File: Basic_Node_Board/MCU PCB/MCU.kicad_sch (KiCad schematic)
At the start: 34 parts, among them J1 Conn_01x02, J2 Conn_01x06_Socket, J3 Conn_01x19_Socket, J4 Conn_01x02_Pin, J5 Conn_01x03_Socket, U2 ESP32-DEVKIT-C, U3 TPS54560BQDDARQ1, U4 AP64060WU-7, U5 AP64060WU-7, U6 TJA1050T/CM,118

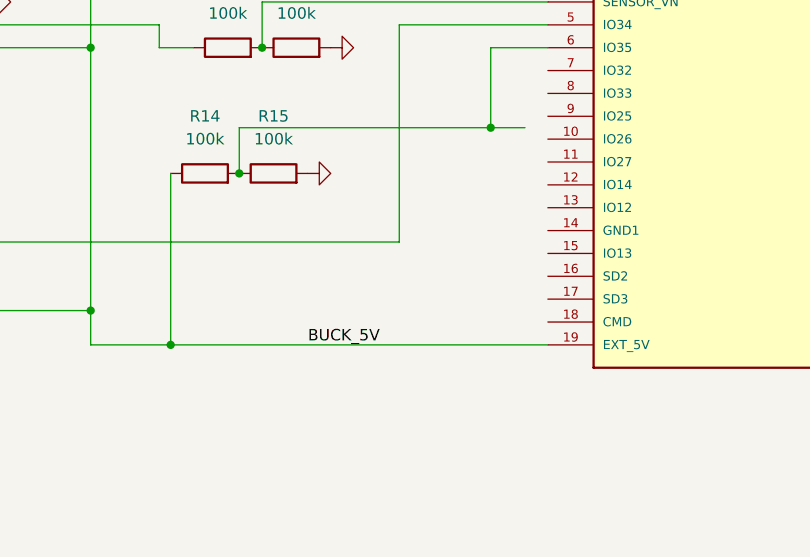
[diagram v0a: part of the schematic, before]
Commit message: made changes to some footprints and overall layout of the board (in line with TI buck recomendations)
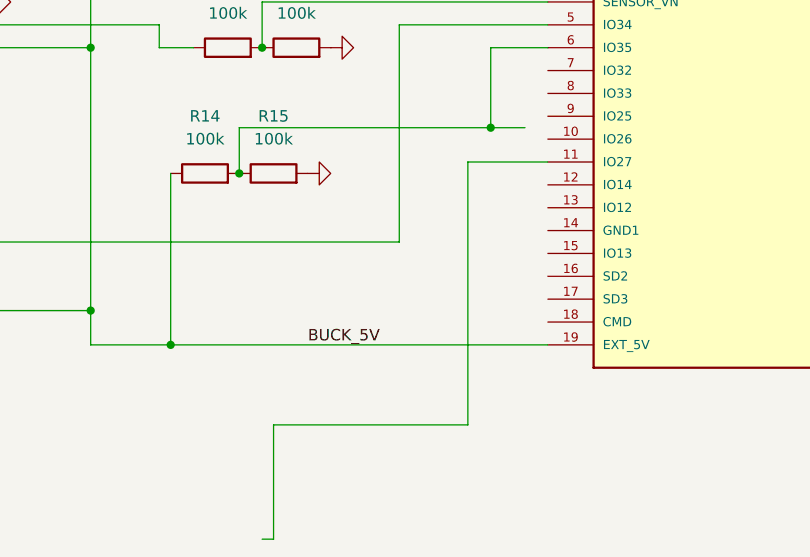
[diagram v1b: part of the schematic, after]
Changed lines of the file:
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@@
+	(wire
+		(pts
+			(xy 100.33 134.62) (xy 91.44 134.62)
+		)
+		(stroke
+			(width 0)
+			(type default)
+		)
+	)
 	(wire
 		(pts
@@
 	(wire
 		(pts
+			(xy 69.85 163.83) (xy 91.44 163.83)
+		)
+		(stroke
+			(width 0)
+			(type default)
+		)
+	)
+	(wire
+		(pts
 			(xy 246.38 46.99) (xy 255.27 46.99)
 		)
@@
 	(wire
 		(pts
+			(xy 91.44 134.62) (xy 91.44 163.83)
+		)
+		(stroke
+			(width 0)
+			(type default)
+		)
+	)
+	(wire
+		(pts
 			(xy 261.62 139.7) (xy 262.89 139.7)
 		)
@@
 	(wire
 		(pts
+			(xy 68.58 176.53) (xy 69.85 176.53)
+		)
+		(stroke
+			(width 0)
+			(type default)
+		)
+	)
+	(wire
+		(pts
 			(xy 57.15 121.92) (xy 57.15 119.38)
 		)
@@
 		)
 		(stroke
+			(width 0)
+			(type default)
+		)
+	)
+	(wire
+		(pts
+			(xy 69.85 163.83) (xy 69.85 176.53)
+		)
+		(stroke

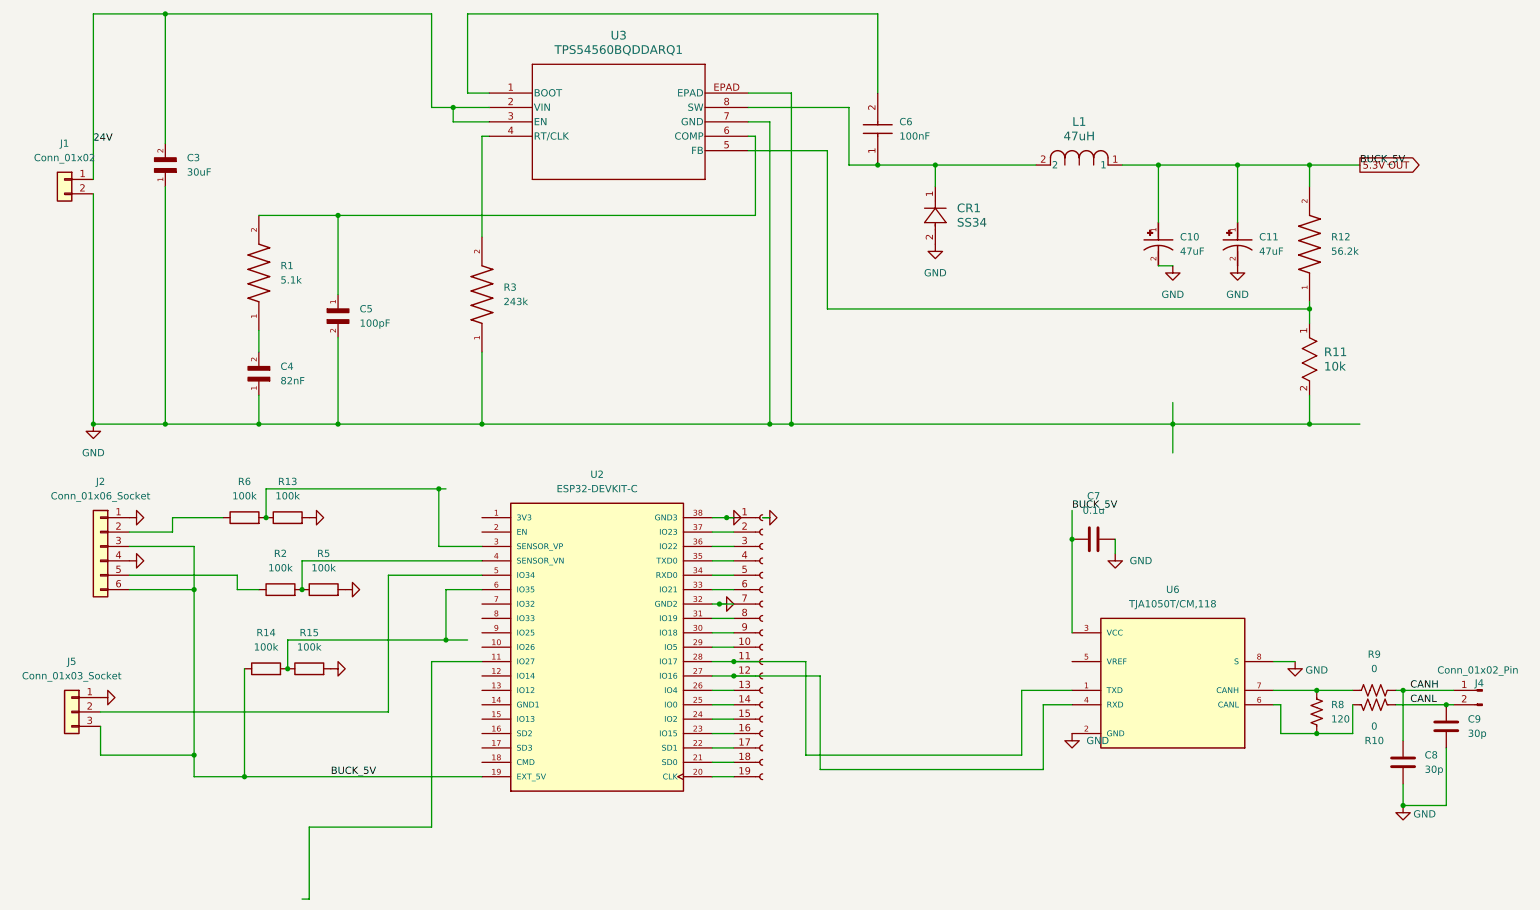
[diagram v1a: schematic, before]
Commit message: fixed the buck converter
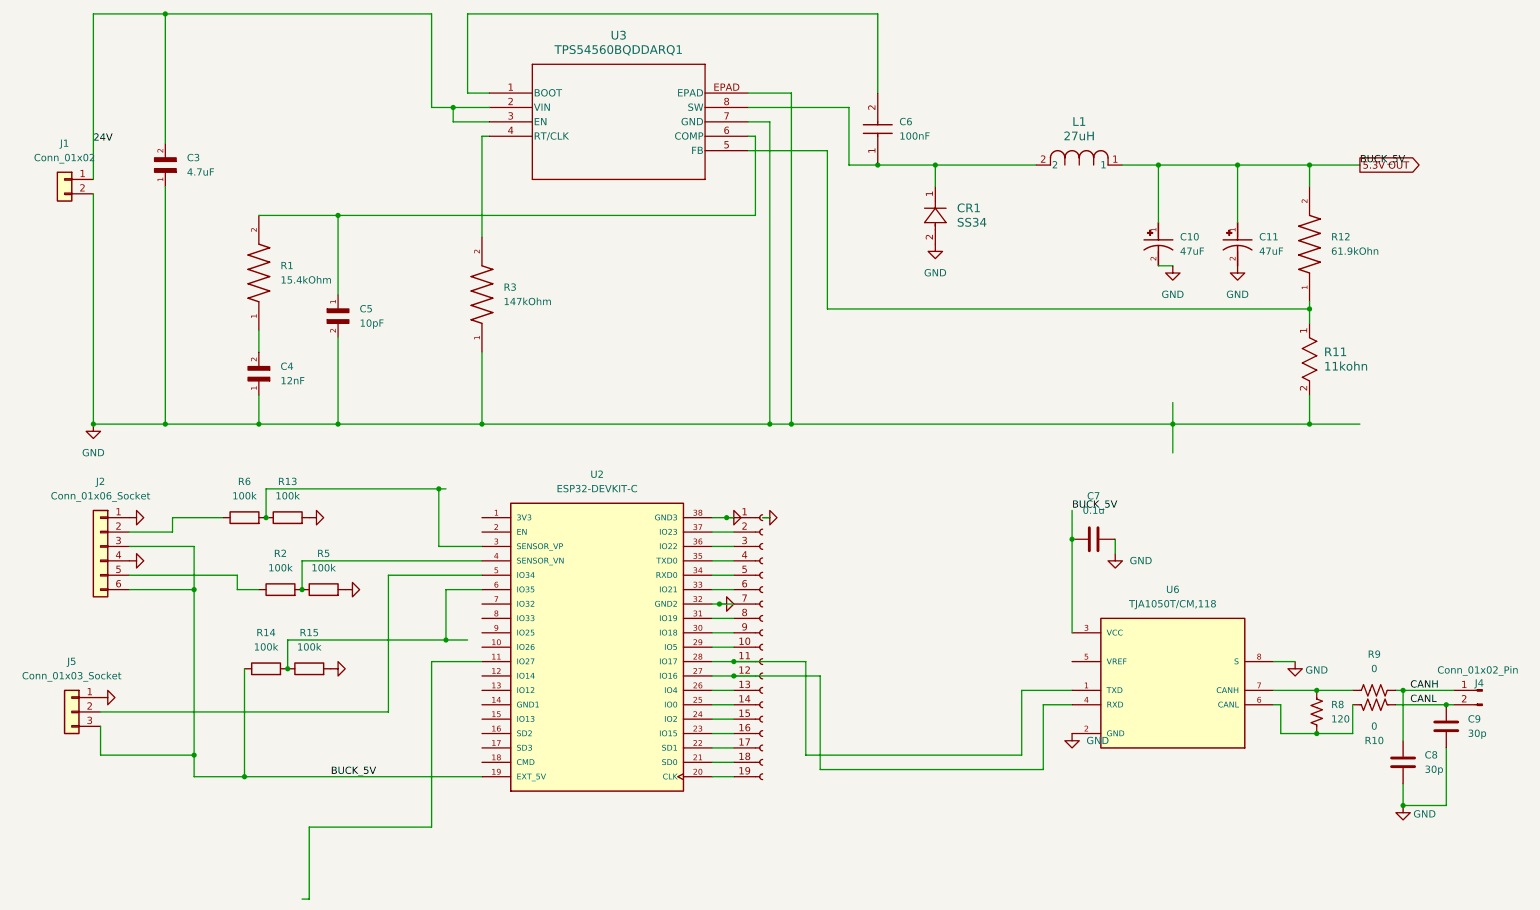
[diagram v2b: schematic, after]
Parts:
- C3: value 30uF -> 4.7uF
- C4: value 82nF -> 12nF
- C5: value 100pF -> 10pF
- L1: value 47uH -> 27uH
- R1: value 5.1k -> 15.4kOhm
- R11: value 10k -> 11kohn
- R12: value 56.2k -> 61.9kOhn
- R3: value 243k -> 147kOhm
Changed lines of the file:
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@@
 			)
 		)
-		(property "Value" "243k"
+		(property "Value" "147kOhm"
 			(at 104.14 71.1199 90)
 			(effects
@@
 			)
 		)
-		(property "Value" "82nF"
+		(property "Value" "12nF"
 			(at 64.77 85.0899 90)
 			(effects
@@
 			)
 		)
-		(property "Value" "100pF"
+		(property "Value" "10pF"
 			(at 78.74 74.9299 90)
 			(effects
@@
 			)
 		)
-		(property "Value" "5.1k"
+		(property "Value" "15.4kOhm"
 			(at 64.77 67.3099 90)
 			(effects
@@
 			)
 		)
-		(property "Value" "30uF"
+		(property "Value" "4.7uF"
 			(at 48.26 48.2599 90)
 			(effects
@@
 			)
 		)
-		(property "Value" "10k"
+		(property "Value" "11kohn"
 			(at 248.92 82.5499 90)
 			(effects
@@
 			)
 		)
-		(property "Value" "47uH"
+		(property "Value" "27uH"
 			(at 205.74 41.91 0)
 			(effects
@@
 			)
 		)
-		(property "Value" "56.2k"
+		(property "Value" "61.9kOhn"
 			(at 250.19 62.2299 90)
 			(effects
